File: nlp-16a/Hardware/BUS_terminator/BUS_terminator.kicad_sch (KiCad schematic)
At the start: 0 parts

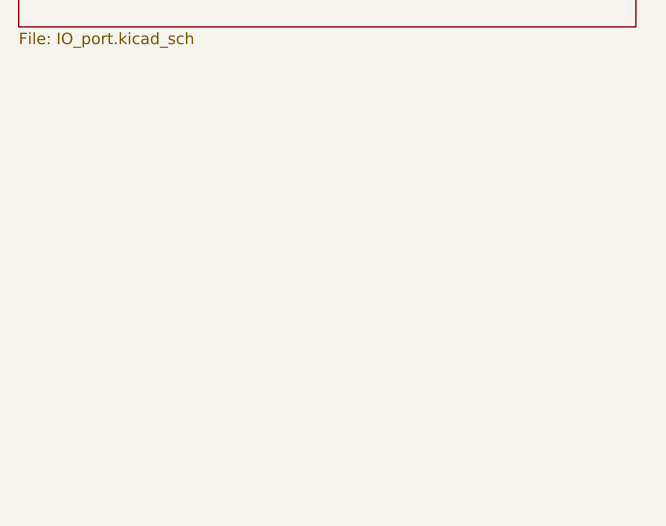
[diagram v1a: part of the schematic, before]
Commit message: バスターミネータのDMA機能は不要と判断したので削除．必要ならば外部回路で実現するように
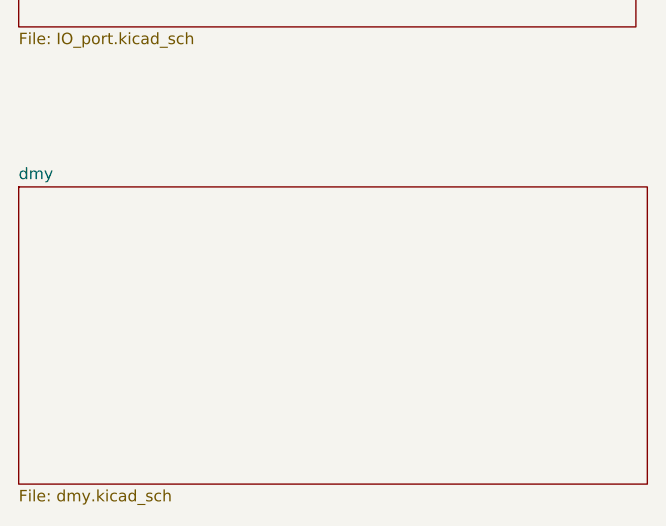
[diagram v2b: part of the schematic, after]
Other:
- added sheet dmy (dmy.kicad_sch)

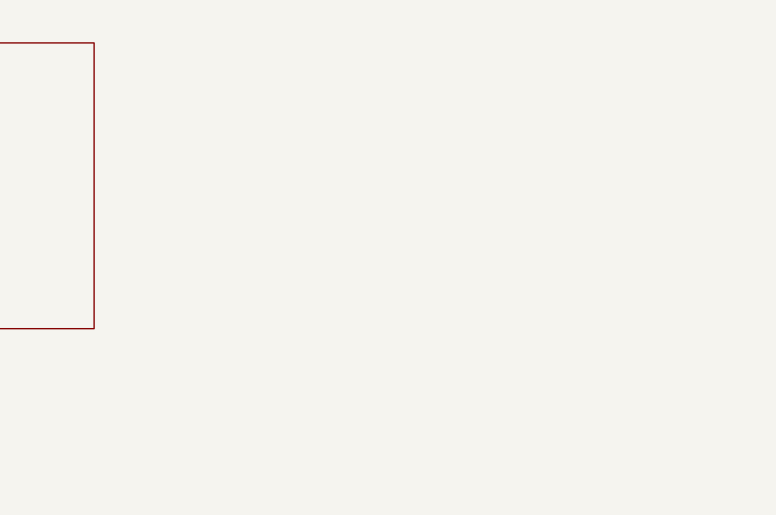
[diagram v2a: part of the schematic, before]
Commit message: v1.1全ガーバーを更新
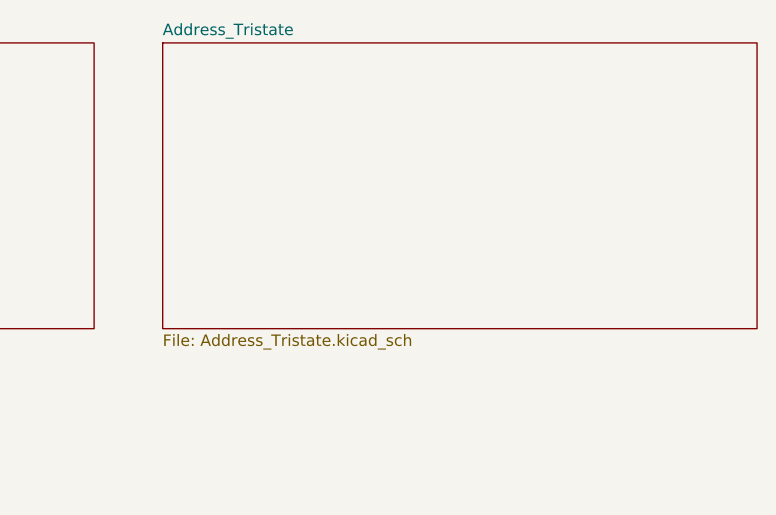
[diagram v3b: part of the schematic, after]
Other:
- added sheet Address_Tristate (Address_Tristate.kicad_sch)
